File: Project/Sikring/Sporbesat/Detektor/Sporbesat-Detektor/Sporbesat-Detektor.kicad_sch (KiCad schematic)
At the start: 14 parts, among them J1 Screw_Terminal_01x02, J2 Screw_Terminal_01x02, J4 Conn_01x05_Socket, Q1 BC857, U1 PC847

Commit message: DCC signal
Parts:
- added R3: 100K, PCM_JLCPCB:R_0805, symbol PCM_JLCPCB-Resistors:0805,1.8kΩ
- C1: value 680nF -> 68nF
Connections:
- net GNDDCC: now also R3.1
- net at C1.1, Q1.3 (C), R2.1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: now also R3.2
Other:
- note added: "Til MCU"
- moved on the sheet: C1, TP1, TP2, TP3

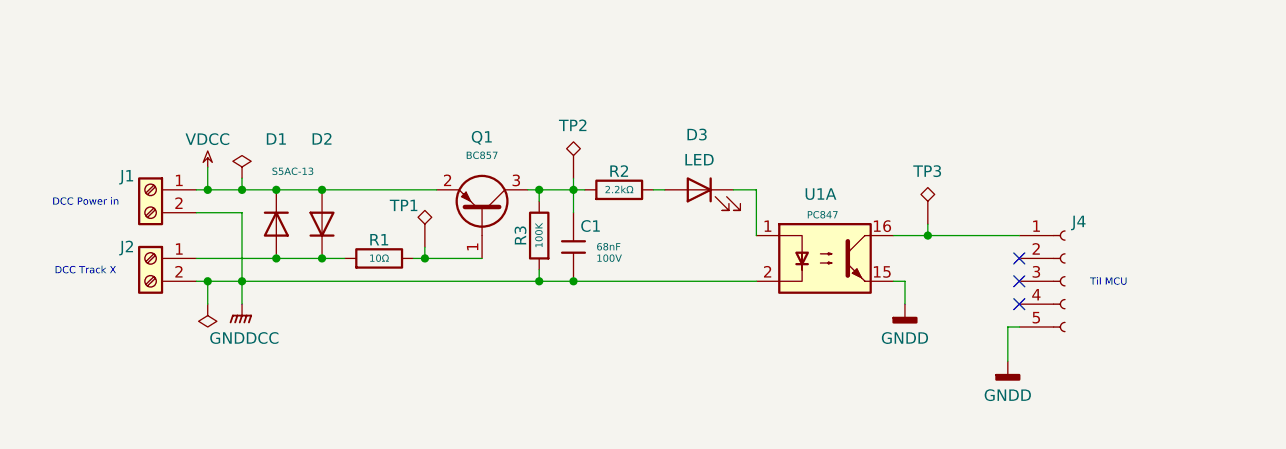
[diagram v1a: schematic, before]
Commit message: CanBus
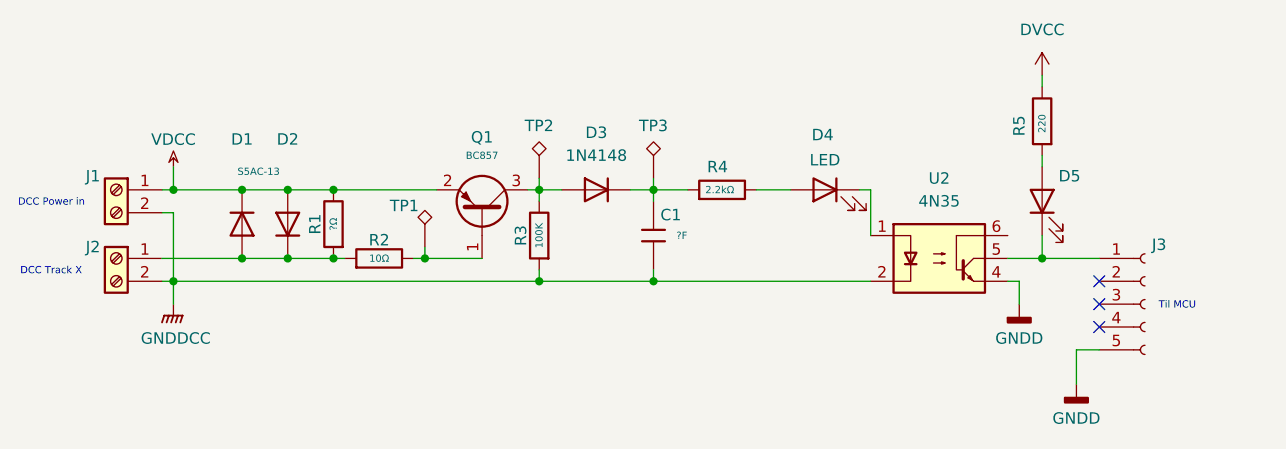
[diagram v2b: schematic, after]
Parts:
- removed U1: PC847, Package_DIP:DIP-16_W7.62mm, symbol Isolator:PC847
- added D3: 1N4148, Diode_THT:D_DO-35_SOD27_P7.62mm_Horizontal, symbol Diode:1N4148
- added D5: LED, LED_SMD:LED_0805_2012Metric, symbol Device:LED
- added R1: ?Ω, PCM_JLCPCB:R_0805, symbol PCM_JLCPCB-Resistors:0805,1.8kΩ
- added R5: 220, PCM_JLCPCB:R_0805, symbol PCM_JLCPCB-Resistors:0805,1.8kΩ
- added U2: 4N35, Package_DIP:DIP-6_W7.62mm, symbol Isolator:4N35
- C1: value 68nF -> ?F
- renumbered D3 to D4, J4 to J3, R1 to R2, R2 to R4
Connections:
- net GNDD: now also U2.4
- net GNDDCC: now also U2.2
- net VDCC: now also R1.2
- net at J3.1 (Pin_1): now also D5.1 (K), U2.5; no longer TP3.1
- net at D4.1 (K): now also U2.1
- net at Q1.3 (C), R3.2, TP2.1: now also D3.2 (A); no longer C1.1, R4.1
- net at D1.2 (A), D2.1 (K), J2.1 (Pin_1)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: now also R1.1
- new net: D5.2 (A), R5.1
- new net: C1.1, D3.1 (K), R4.1, TP3.1
- new net DVCC: R5.2
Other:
- moved on the sheet: C1, D1, D2, D4, J1, J2, J3, R4, TP2
